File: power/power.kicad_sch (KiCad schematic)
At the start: 12 parts, among them J1 GPIO, J2 PWM_OUT, J3 PWM_IN, J4 JP_EXT, J5 JP_VOLTS, J8 PWM_OUT, Q1 D15P05

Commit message: solder pads
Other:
- note added: "GPIO0, GPIO1, GPIO4, GPIO5, GPIO7, GPIO14, GPIO16, GPIO22, GPIO23 and GPIO26, GPIO27"
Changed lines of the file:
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@@
+		)
+	)
+	(text "GPIO0, GPIO1, GPIO4, GPIO5, \nGPIO7, GPIO14, GPIO16, GPIO22, \nGPIO23 and GPIO26, GPIO27"
+		(exclude_from_sim no)
+		(at 227.076 67.818 0)
+		(effects
+			(font
+				(size 1.27 1.27)
+			)
 		)
 	)

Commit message: lots of changes
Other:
- note removed: "GPIO0, GPIO1, GPIO4, GPIO5, GPIO7, GPIO14, GPIO16, GPIO22, GPIO23 and GPIO26, GPIO27"
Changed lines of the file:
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@@
-		)
-	)
-	(text "GPIO0, GPIO1, GPIO4, GPIO5, \nGPIO7, GPIO14, GPIO16, GPIO22, \nGPIO23 and GPIO26, GPIO27"
-		(exclude_from_sim no)
-		(at 227.076 67.818 0)
-		(effects
-			(font
-				(size 1.27 1.27)
-			)
 		)
 	)

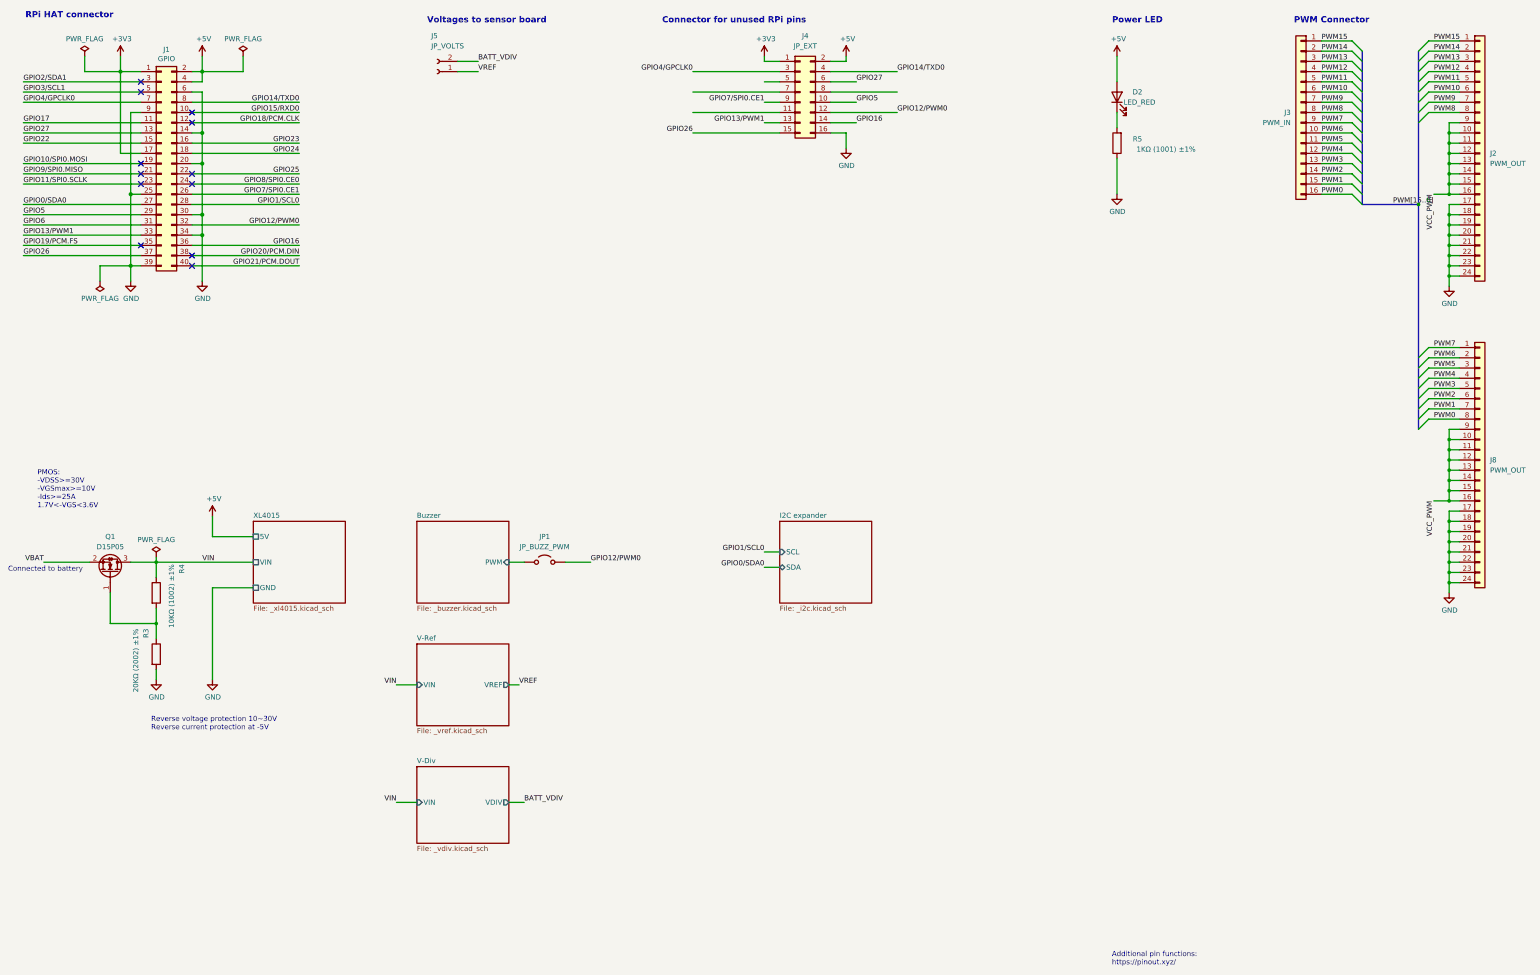
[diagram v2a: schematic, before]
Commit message: use TPS56A37 (preliminary commit with broken net tie via)
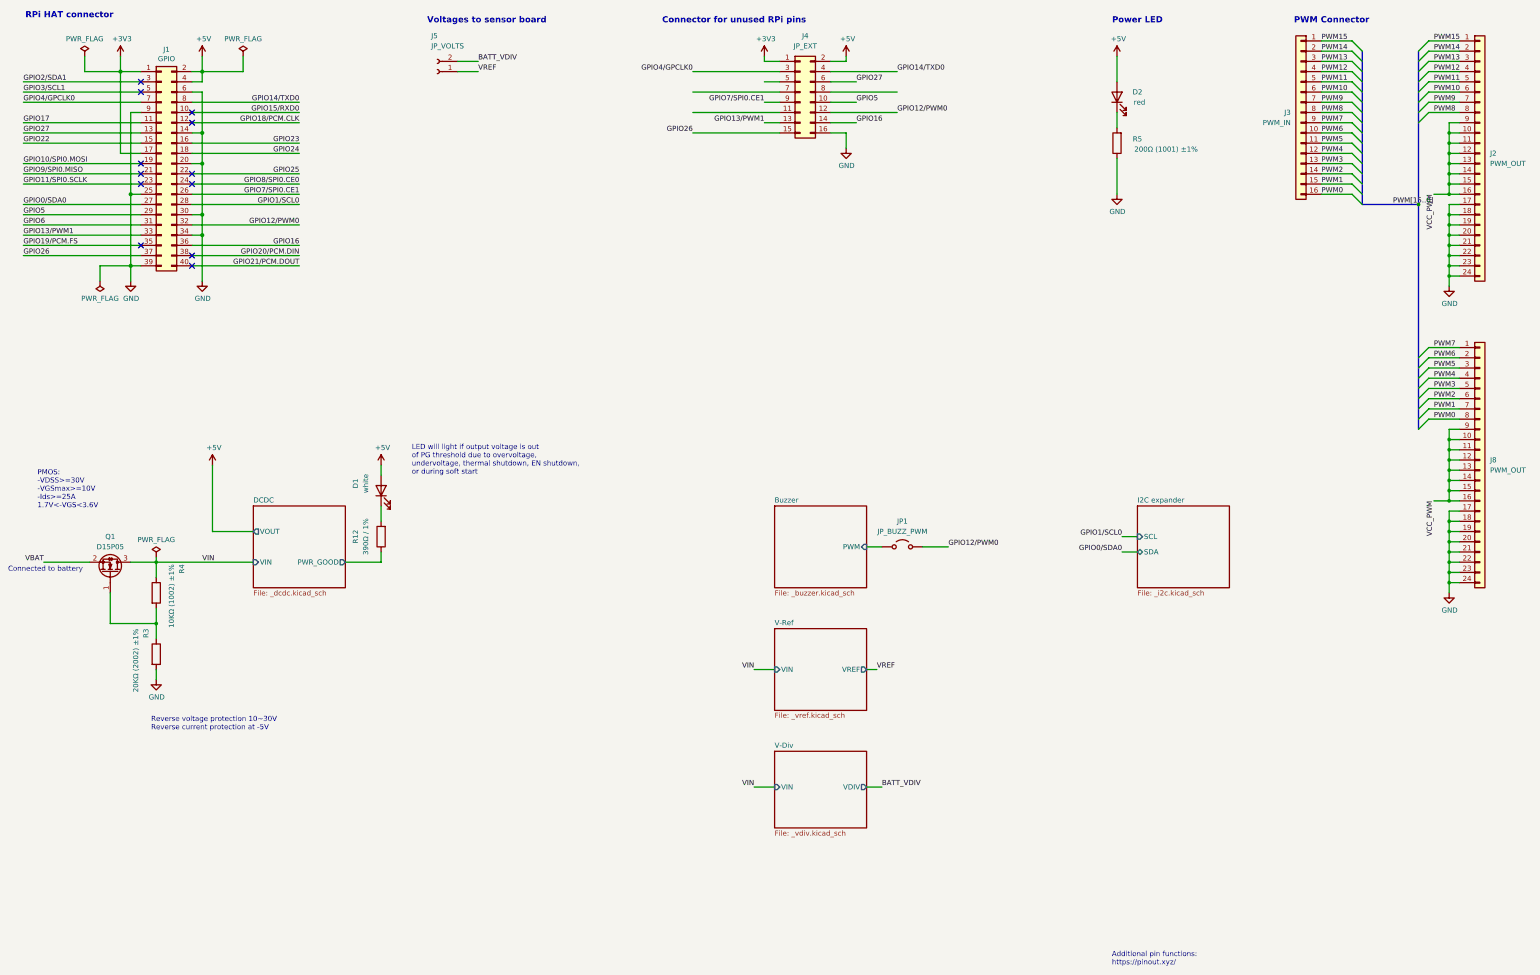
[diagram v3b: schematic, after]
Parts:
- added D1: white, LED_SMD:LED_0603_1608Metric, symbol Device:LED
- added R12: 390Ω / 1%, Resistor_SMD:R_0603_1608Metric, symbol Device:R
- D2: value LED_RED -> red
- R5: value 1KΩ (1001) ±1% -> 200Ω (1001) ±1%; footprint Resistor_SMD:R_0402_1005Metric -> Resistor_SMD:R_0603_1608Metric; Part 0402WGF1001TCE -> 0603WAF2000T5E
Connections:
- net +5V: now also D1.2 (A)
- new net: D1.1 (K), R12.2
- new net DCDC/PWR_GOOD: R12.1
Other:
- removed sheet XL4015
- added sheet DCDC (_dcdc.kicad_sch)
- note added: "LED will light if output voltage is out of PG threshold due to overvoltage, undervoltage, thermal shutdown, EN shutdown, or during soft start"
- moved on the sheet: JP1

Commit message: add two solder pins for VCC_PWM; place DCDC/Vin
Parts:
- added J18, J9: JP_VCC_PWM, Connector_PinHeader_2.54mm:PinHeader_1x01_P2.54mm_Vertical, symbol Connector_Generic:Conn_01x01
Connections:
- net VCC_PWM: now also J18.1 (Pin_1), J9.1 (Pin_1)
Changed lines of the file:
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@@
 	)
 	(junction
+		(at 356.87 93.98)
+		(diameter 0)
+		(color 0 0 0 0)
+	)
+	(junction
 		(at 386.08 151.13)
 		(diameter 0)
@@
 	(wire
 		(pts
+			(xy 356.87 93.98) (xy 354.33 93.98)
+		)
+		(stroke
+			(width 0)
+			(type default)
+		)
+	)
+	(wire
+		(pts
 			(xy 46.99 33.02) (xy 46.99 36.83)
 		)
@@
 	(wire
 		(pts
+			(xy 354.33 85.09) (xy 356.87 85.09)
+		)
+		(stroke
+			(width 0)
+			(type default)
+		)
+	)
+	(wire
+		(pts
 			(xy 46.99 36.83) (xy 55.88 36.83)
 		)
@@
 	(wire
 		(pts
+			(xy 356.87 85.09) (xy 356.87 93.98)
+		)
+		(stroke
+			(width 0)
+			(type default)
+		)
+	)
+	(wire
+		(pts
 			(xy 386.08 52.07) (xy 388.62 52.07)
 		)
@@
 	(wire
 		(pts
+			(xy 356.87 93.98) (xy 367.03 93.98)
+		)
+		(stroke
+			(width 0)
+			(type default)
+		)
+	)
+	(wire
+		(pts
 			(xy 386.08 72.39) (xy 386.08 74.93)
 		)
@@
 		)
 	)
+	(label "VCC_PWM"
+		(at 367.03 93.98 0)
+		(effects
+			(font
+				(size 1.27 1.27)
+			)
+			(justify left bottom)
+		)
+	)
 	(label "BATT_VDIV"
 		(at 245.11 214.63 0)
@@
 	)
 	(symbol
+		(lib_id "Connector_Generic:Conn_01x01")
+		(at 349.25 93.98 180)
+		(unit 1)
+		(body_style 1)
+		(exclude_from_sim no)
+		(in_bom no)
+		(on_board yes)
+		(in_pos_files yes)
+		(dnp yes)
+		(property "Reference" "J18"
+			(at 348.996 90.932 0)
+			(show_name no)
+			(do_not_autoplace no)
+			(effects
+				(font
+					(size 1.27 1.27)
+				)
+			)
+		)
+		(property "Value" "JP_VCC_PWM"
+			(at 344.678 88.9 0)
+			(show_name no)
+			(do_not_autoplace no)
+			(effects
+				(font
+					(size 1.27 1.27)
+				)
+			)
+		)
+		(property "Footprint" "Connector_PinHeader_2.54mm:PinHeader_1x01_P2.54mm_Vertical"
+			(at 349.25 93.98 0)
+			(hide yes)
+			(show_name no)
+			(do_not_autoplace no)
+			(effects
+				(font
+					(size 1.27 1.27)
+				)
+			)
+		)
+		(property "Datasheet" ""
+			(at 349.25 93.98 0)
+			(hide yes)
+			(show_name no)
+			(do_not_autoplace no)
+			(effects
+				(font
+					(size 1.27 1.27)
+				)
+			)
+		)
+		(property "Description" "Generic connector, single row, 01x01, script generated (kicad-library-utils/schlib/autogen/connector/)"
+			(at 349.25 93.98 0)
+			(hide yes)
+			(show_name no)
+			(do_not_autoplace no)
+			(effects
+				(font
+					(size 1.27 1.27)
+				)
+			)
+		)
+		(property "Part" ""
+			(at 349.25 93.98 0)
+			(hide yes)
+			(show_name no)
+			(do_not_autoplace no)
+			(effects
+				(font
+					(size 1.27 1.27)
+				)
+			)
+		)
+		(pin "1"
+		)
+		(instances
+			(project "power"
+				(path "/e63e39d7-6ac0-4ffd-8aa3-1841a4541b55"
+					(reference "J18")
+					(unit 1)
+				)
+			)
+		)
+	)
+	(symbol
 		(lib_id "Connector_Generic:Conn_01x16")
 		(at 349.25 46.99 0)
@@
 					(unit 1)
 				)
+			)
+		)
+	)
+	(symbol
+		(lib_id "Connector_Generic:Conn_01x01")
+		(at 349.25 85.09 180)
+		(unit 1)
+		(body_style 1)
+		(exclude_from_sim no)
+		(in_bom no)
+		(on_board yes)
+		(in_pos_files yes)
+		(dnp yes)
+		(property "Reference" "J9"
+			(at 349.504 82.042 0)
+			(show_name no)
+			(do_not_autoplace no)
+			(effects
+				(font
+					(size 1.27 1.27)
+				)
+			)
+		)
+		(property "Value" "JP_VCC_PWM"
+			(at 344.678 80.01 0)
+			(show_name no)
+			(do_not_autoplace no)
+			(effects
+				(font
+					(size 1.27 1.27)
+				)
+			)
+		)
+		(property "Footprint" "Connector_PinHeader_2.54mm:PinHeader_1x01_P2.54mm_Vertical"
+			(at 349.25 85.09 0)
+			(hide yes)
+			(show_name no)
+			(do_not_autoplace no)
+			(effects
+				(font
+					(size 1.27 1.27)
+				)
+			)
+		)
+		(property "Datasheet" ""
+			(at 349.25 85.09 0)
+			(hide yes)
+			(show_name no)
+			(do_not_autoplace no)
+			(effects
+				(font
+					(size 1.27 1.27)
+				)
+			)
+		)
+		(property "Description" "Generic connector, single row, 01x01, script generated (kicad-library-utils/schlib/autogen/connector/)"
+			(at 349.25 85.09 0)
+			(hide yes)
+			(show_name no)
+			(do_not_autoplace no)
+			(effects
+				(font
+					(size 1.27 1.27)
+				)
+			)
+		)
+		(property "Part" ""
+			(at 349.25 85.09 0)
+			(hide yes)
+			(show_name no)
+			(do_not_autoplace no)
+			(effects
+				(font
+					(size 1.27 1.27)
+				)
+			)
+		)
+		(pin "1"
+		)
+		(instances
+			(project "power"
+				(path "/e63e39d7-6ac0-4ffd-8aa3-1841a4541b55"
+					(reference "J9")
+					(unit 1)
+				)

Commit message: use normally closed solder jumper for buzzer/pwm selection
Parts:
- JP1: footprint Connector_PinHeader_2.54mm:PinHeader_1x02_P2.54mm_Vertical -> Jumper:SolderJumper-2_P1.3mm_Bridged2Bar_RoundedPad1.0x1.5mm
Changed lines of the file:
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@@
 			)
 		)
-		(property "Footprint" "Connector_PinHeader_2.54mm:PinHeader_1x02_P2.54mm_Vertical"
+		(property "Footprint" "Jumper:SolderJumper-2_P1.3mm_Bridged2Bar_RoundedPad1.0x1.5mm"
 			(at 250.19 154.94 0)
 			(hide yes)

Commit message: power jumper for i2c extender (default 3V3); preliminary RS485 transceiver
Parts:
- added J19: Conn_01x01, Connector_Wire:SolderWirePad_1x01_SMD_1.5x3mm, symbol Connector_Generic:Conn_01x01
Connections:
- net GPIO12/PWM0: no longer J4.12 (Pin_12)
- net GPIO13/PWM1: no longer J4.13 (Pin_13)
- net GPIO14/TXD0: no longer J4.4 (Pin_4)
- net GPIO16: no longer J4.14 (Pin_14)
- net GPIO26: no longer J4.15 (Pin_15)
- net GPIO27: no longer J4.6 (Pin_6)
- net GPIO4/GPCLK0: no longer J4.3 (Pin_3)
- net GPIO5: no longer J4.10 (Pin_10)
- net GPIO7/SPI0.CE1: no longer J4.9 (Pin_9)
- net VBAT: now also J19.1 (Pin_1)
- no-connect marks 12 -> 25
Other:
- added sheet RS485 (_rs485.kicad_sch)

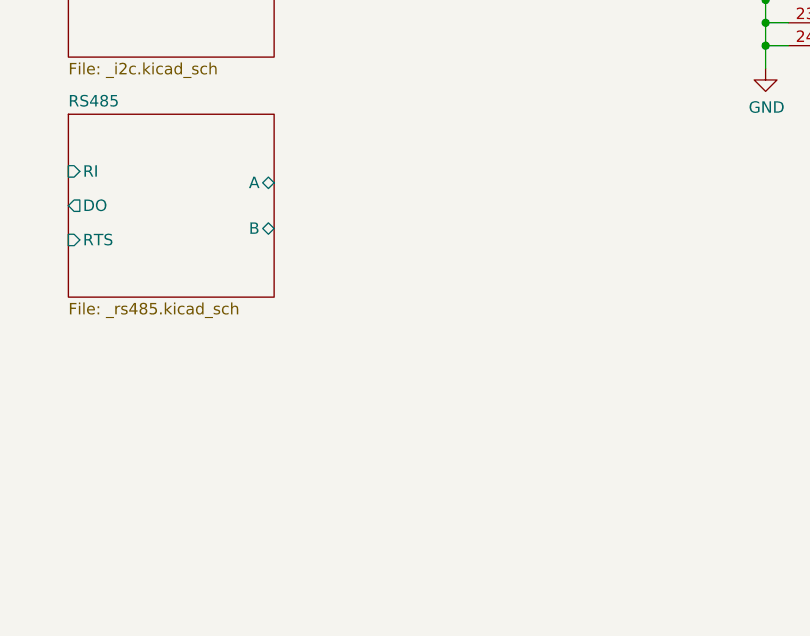
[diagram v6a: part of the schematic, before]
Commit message: routing of RS485 transceiver
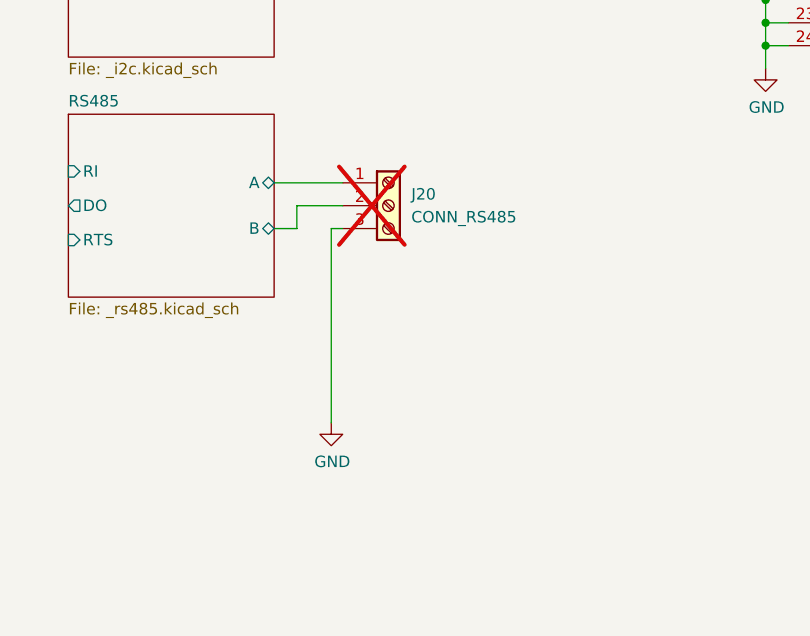
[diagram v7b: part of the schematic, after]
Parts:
- added J20: CONN_RS485, Connector_Phoenix_MC:PhoenixContact_MC_1,5_3-G-3.5_1x03_P3.50mm_Horizontal, symbol Connector:Screw_Terminal_01x03
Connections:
- net GND: now also J20.3 (Pin_3)
- net RS485/A: now also J20.1 (Pin_1)
- net RS485/B: now also J20.2 (Pin_2)
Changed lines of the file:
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@@
 	(wire
 		(pts
+			(xy 331.47 179.07) (xy 339.09 179.07)
+		)
+		(stroke
+			(width 0)
+			(type default)
+		)
+	)
+	(wire
+		(pts
 			(xy 386.08 82.55) (xy 388.62 82.55)
 		)
@@
 	(wire
 		(pts
+			(xy 337.82 184.15) (xy 337.82 205.74)
+		)
+		(stroke
+			(width 0)
+			(type default)
+		)
+	)
+	(wire
+		(pts
 			(xy 232.41 46.99) (xy 248.92 46.99)
 		)
@@
 	(wire
 		(pts
+			(xy 331.47 184.15) (xy 334.01 184.15)
+		)
+		(stroke
+			(width 0)
+			(type default)
+		)
+	)
+	(wire
+		(pts
 			(xy 381 105.41) (xy 388.62 105.41)
 		)
@@
 	(wire
 		(pts
+			(xy 339.09 184.15) (xy 337.82 184.15)
+		)
+		(stroke
+			(width 0)
+			(type default)
+		)
+	)
+	(wire
+		(pts
 			(xy 213.36 185.42) (xy 218.44 185.42)
 		)
@@
 	(wire
 		(pts
+			(xy 334.01 184.15) (xy 334.01 181.61)
+		)
+		(stroke
+			(width 0)
+			(type default)
+		)
+	)
+	(wire
+		(pts
 			(xy 76.2 77.47) (xy 73.66 77.47)
 		)
@@
 	(wire
 		(pts
+			(xy 334.01 181.61) (xy 339.09 181.61)
+		)
+		(stroke
+			(width 0)
+			(type default)
+		)
+	)
+	(wire
+		(pts
 			(xy 76.2 72.39) (xy 73.66 72.39)
 		)
@@
 	)
 	(symbol
+		(lib_id "Connector:Screw_Terminal_01x03")
+		(at 344.17 181.61 0)
+		(unit 1)
+		(body_style 1)
+		(exclude_from_sim no)
+		(in_bom no)
+		(on_board yes)
+		(in_pos_files no)
+		(dnp yes)
+		(fields_autoplaced yes)
+		(property "Reference" "J20"
+			(at 346.71 180.3399 0)
+			(show_name no)
+			(do_not_autoplace no)
+			(effects
+				(font
+					(size 1.27 1.27)
+				)
+				(justify left)
+			)
+		)
+		(property "Value" "CONN_RS485"
+			(at 346.71 182.8799 0)
+			(show_name no)
+			(do_not_autoplace no)
+			(effects
+				(font
+					(size 1.27 1.27)
+				)
+				(justify left)
+			)
+		)
+		(property "Footprint" "Connector_Phoenix_MC:PhoenixContact_MC_1,5_3-G-3.5_1x03_P3.50mm_Horizontal"
+			(at 344.17 181.61 0)
+			(hide yes)
+			(show_name no)
+			(do_not_autoplace no)
+			(effects
+				(font
+					(size 1.27 1.27)
+				)
+			)
+		)
+		(property "Datasheet" ""
+			(at 344.17 181.61 0)
+			(hide yes)
+			(show_name no)
+			(do_not_autoplace no)
+			(effects
+				(font
+					(size 1.27 1.27)
+				)
+			)
+		)
+		(property "Description" "Generic screw terminal, single row, 01x03, script generated (kicad-library-utils/schlib/autogen/connector/)"
+			(at 344.17 181.61 0)
+			(hide yes)
+			(show_name no)
+			(do_not_autoplace no)
+			(effects
+				(font
+					(size 1.27 1.27)
+				)
+			)
+		)
+		(property "Part" ""
+			(at 344.17 181.61 0)
+			(hide yes)
+			(show_name no)
+			(do_not_autoplace no)
+			(effects
+				(font
+					(size 1.27 1.27)
+				)
+			)
+		)
+		(pin "1"
+		)
+		(pin "2"
+		)
+		(pin "3"
+		)
+		(instances
+			(project "power"
+				(path "/e63e39d7-6ac0-4ffd-8aa3-1841a4541b55"
+					(reference "J20")
+					(unit 1)
+				)
+			)
+		)
+	)
+	(symbol
 		(lib_id "power:GND")
 		(at 236.22 55.88 0)
@@
 					(unit 1)
 				)
+			)
+		)
+	)
+	(symbol
+		(lib_id "power:GND")
+		(at 337.82 205.74 0)
+		(unit 1)
+		(body_style 1)
+		(exclude_from_sim no)
+		(in_bom yes)
+		(on_board yes)
+		(in_pos_files yes)
+		(dnp no)
+		(property "Reference" "#PWR019"
+			(at 337.82 212.09 0)
+			(hide yes)
+			(show_name no)
+			(do_not_autoplace no)
+			(effects
+				(font
+					(size 1.27 1.27)
+				)
+			)
+		)
+		(property "Value" "GND"
+			(at 337.9343 210.0644 0)
+			(show_name no)
+			(do_not_autoplace no)
+			(effects
+				(font
+					(size 1.27 1.27)
+				)
+			)
+		)
+		(property "Footprint" ""
+			(at 337.82 205.74 0)
+			(show_name no)
+			(do_not_autoplace no)
+			(effects
+				(font
+					(size 1.27 1.27)
+				)
+			)
+		)
+		(property "Datasheet" ""
+			(at 337.82 205.74 0)
+			(show_name no)
+			(do_not_autoplace no)
+			(effects
+				(font
+					(size 1.27 1.27)
+				)
+			)
+		)
+		(property "Description" "Power symbol creates a global label with name \"GND\" , ground"
+			(at 337.82 205.74 0)
+			(hide yes)
+			(show_name no)
+			(do_not_autoplace no)
+			(effects
+				(font
+					(size 1.27 1.27)
+				)
+			)
+		)
+		(pin "1"
+		)
+		(instances
+			(project "power"
+				(path "/e63e39d7-6ac0-4ffd-8aa3-1841a4541b55"
+					(reference "#PWR019")
+					(unit 1)
+				)
